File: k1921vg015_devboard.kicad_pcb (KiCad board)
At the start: 4 copper layers, 79.5 x 70 mm, 46 parts, among them J1 Conn_02x25_Odd_Even, J2 Conn_02x25_Odd_Even, J3 Conn_02x06_Odd_Even, J4 Conn_02x01, J7 USB_C_Receptacle_USB2.0_16P, U1 AMS1117-3.3, U2 TL432DBZ, Y2 Crystal, Y3 Crystal

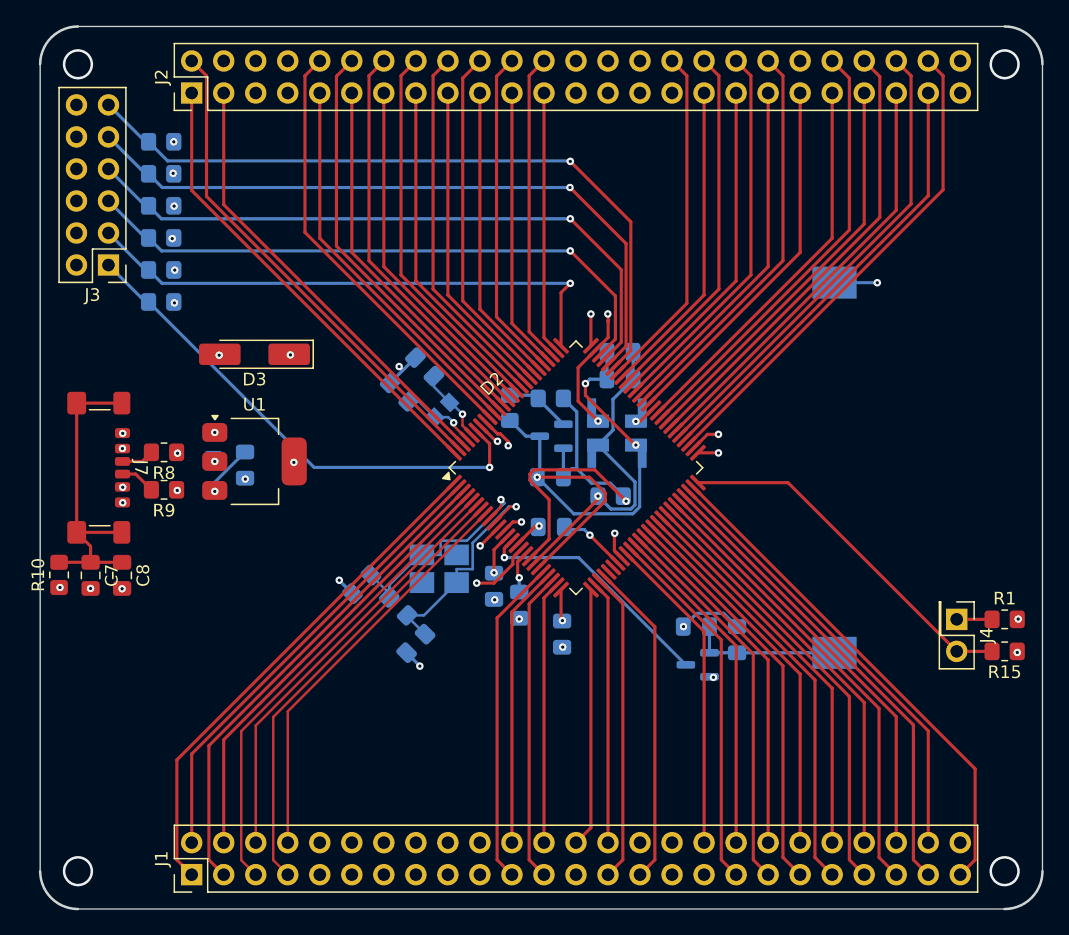
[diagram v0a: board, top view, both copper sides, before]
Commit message: add silkscreen
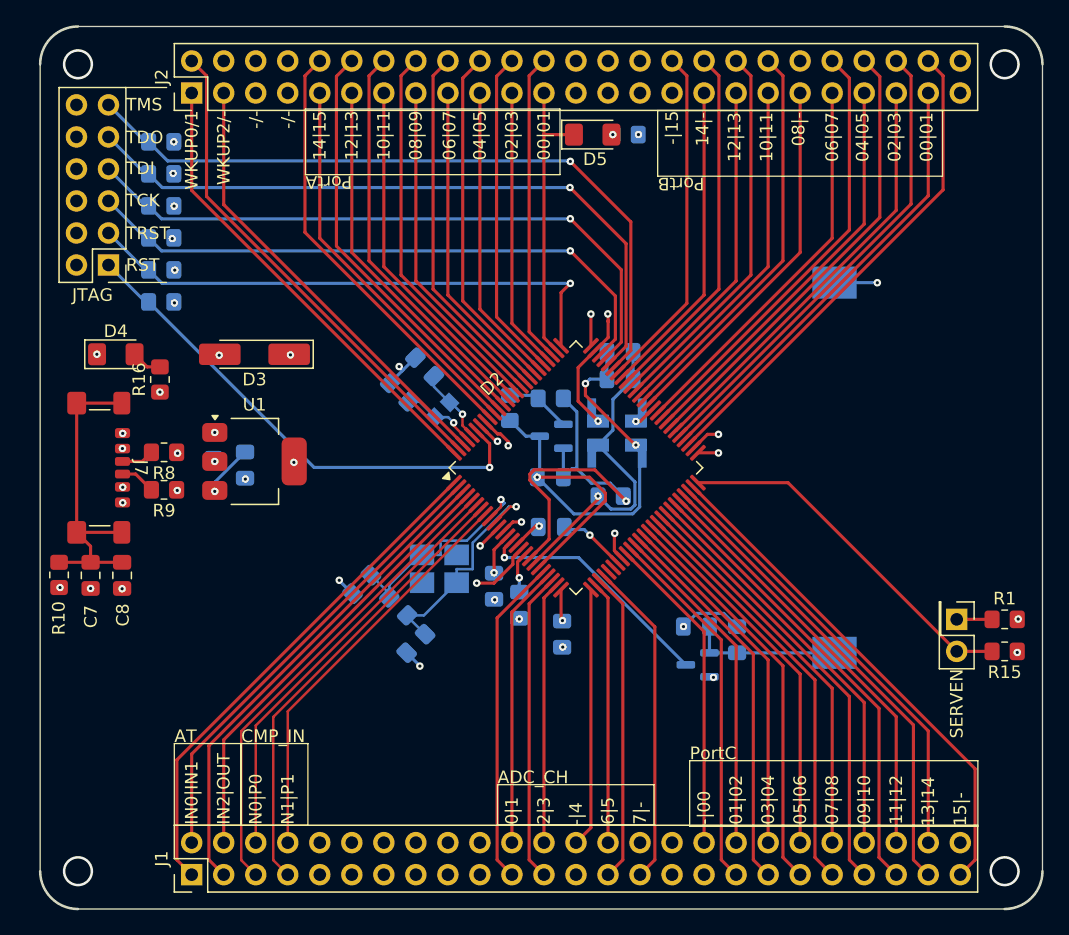
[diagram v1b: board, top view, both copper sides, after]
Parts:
- added D4: LED, LED_SMD:LED_1206_3216Metric_Pad1.42x1.75mm_HandSolder, F.Cu at (6.00, -9.00)
- added D5: LED, LED_SMD:LED_1206_3216Metric_Pad1.42x1.75mm_HandSolder, F.Cu at (43.8, -26.4)
- added R16: 1k, Resistor_SMD:R_0805_2012Metric_Pad1.20x1.40mm_HandSolder, F.Cu at (9.50, -7.00)
- added R17: 1k, Resistor_SMD:R_0805_2012Metric_Pad1.20x1.40mm_HandSolder, B.Cu at (46.4, -26.4)
- renumbered J3 to JTAG, J4 to SERVEN
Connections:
- J2 pad 5: unconnected-(J2-Pin_5-Pad5) -> 5V
- J2 pad 6: unconnected-(J2-Pin_6-Pad6) -> GND
- J2 pad 7: unconnected-(J2-Pin_7-Pad7) -> +3V3
- J2 pad 8: unconnected-(J2-Pin_8-Pad8) -> GND
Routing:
- net 5V: track 4.27 -> 37.4 mm, vias 3 -> 4
- net Net-(D4-A): track 0.00 -> 2.43 mm
- net /PA0: track 20.8 -> 23.1 mm
- net Net-(D5-A): track 0.00 -> 0.16 mm, vias 0 -> 1
- net +3V3: vias 16 -> 17
- net GND: track 38.2 -> 38.3 mm, vias 31 -> 32
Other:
- board text added: "-/-"
- board text added: "-|00"
- board text added: "-|15"
- board text added: "-|4"
- board text added: "00|01"
- board text added: "01|02"
- board text added: "02|03"
- board text added: "03|04"
- board text added: "04|05"
- board text added: "05|06"
- board text added: "06|07"
- board text added: "07|08"
- board text added: "08|-"
- board text added: "08|09"
- board text added: "09|10"
- board text added: "0|1"
- board text added: "10|11"
- board text added: "11|12"
- board text added: "12|13"
- board text added: "13|14"
- board text added: "14|-"
- board text added: "14|15"
- board text added: "15|-"
- board text added: "2|3"
- board text added: "6|5"
- board text added: "7|-"
- board text added: "ADC_CH"
- board text added: "AT"
- board text added: "BAT54C"
- board text added: "CMP_IN"
- board text added: "IN0|IN1"
- board text added: "IN2|OUT"
- board text added: "N0|P0"
- board text added: "N1|P1"
- board text added: "PortA"
- board text added: "PortB"
- board text added: "PortC"
- board text added: "RST"
- board text added: "TCK"
- board text added: "TDI"
- board text added: "TDO"
- board text added: "TMS"
- board text added: "TRST"
- board text added: "WKUP0/1"
- board text added: "WKUP2/-"
